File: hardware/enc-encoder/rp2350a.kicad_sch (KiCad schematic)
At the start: 31 parts, among them U1 RP2350A, U2 W25Q128JVS, Y1 ABM8-272-T3

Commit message: Needs checking and ERC fix
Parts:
- added TP1, TP2, TP3: SPARE_GPIO, TestPoint:TestPoint_Pad_1.0x1.0mm, symbol Connector:TestPoint
- renumbered C15 to C10, C12 to C11, C13 to C12, C14 to C13, C2 to C14, C1 to C15, C11 to C16, C9 to C17, C8 to C18, C21 to C20, C18 to C21, C20 to C22, C16 to C23, C17 to C24, C22 to C9, R13 to R12, R6 to R13, R12 to R14, R7 to R15, R15 to R16, R4 to R17, R5 to R18, R14 to R19, R3 to R20, U2 to U4, U1 to U5
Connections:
- net GPIO_0 is gone; now on net RP_I2C_SDA: R14.2
- net RP_HALL_DIR: now reaches U5.10 (GPIO7)
- net RP_ID_ADDR2: now reaches U5.12 (GPIO8)
- net RP_ID_ADDR1: now reaches U5.13 (GPIO9)
- net RP_ID_ADDR0: now reaches U5.14 (GPIO10)
- net at U5.15 (GPIO11): now also TP1.1
- net at U5.16 (GPIO12): now also TP2.1
- net at U5.17 (GPIO13): now also TP3.1
- net RP_I2C_SDA: now reaches U5.2 (GPIO0)
- net RP_I2C_SCL: now reaches U5.3 (GPIO1)
- net RP_RS485_RX: now reaches U5.4 (GPIO2)
- net RP_HALL_AOUT: now reaches U5.40 (GPIO26/ADC0)
- net RP_RS485_TX: now reaches U5.5 (GPIO3)
- net RP_RS485_DIR: now reaches U5.7 (GPIO4)
- net RP_STATUS_LED: now reaches U5.8 (GPIO5)
- net RP_HALL_PGO: now reaches U5.9 (GPIO6)
- no-connect marks 0 -> 15
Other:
- note added: "Flash mem"

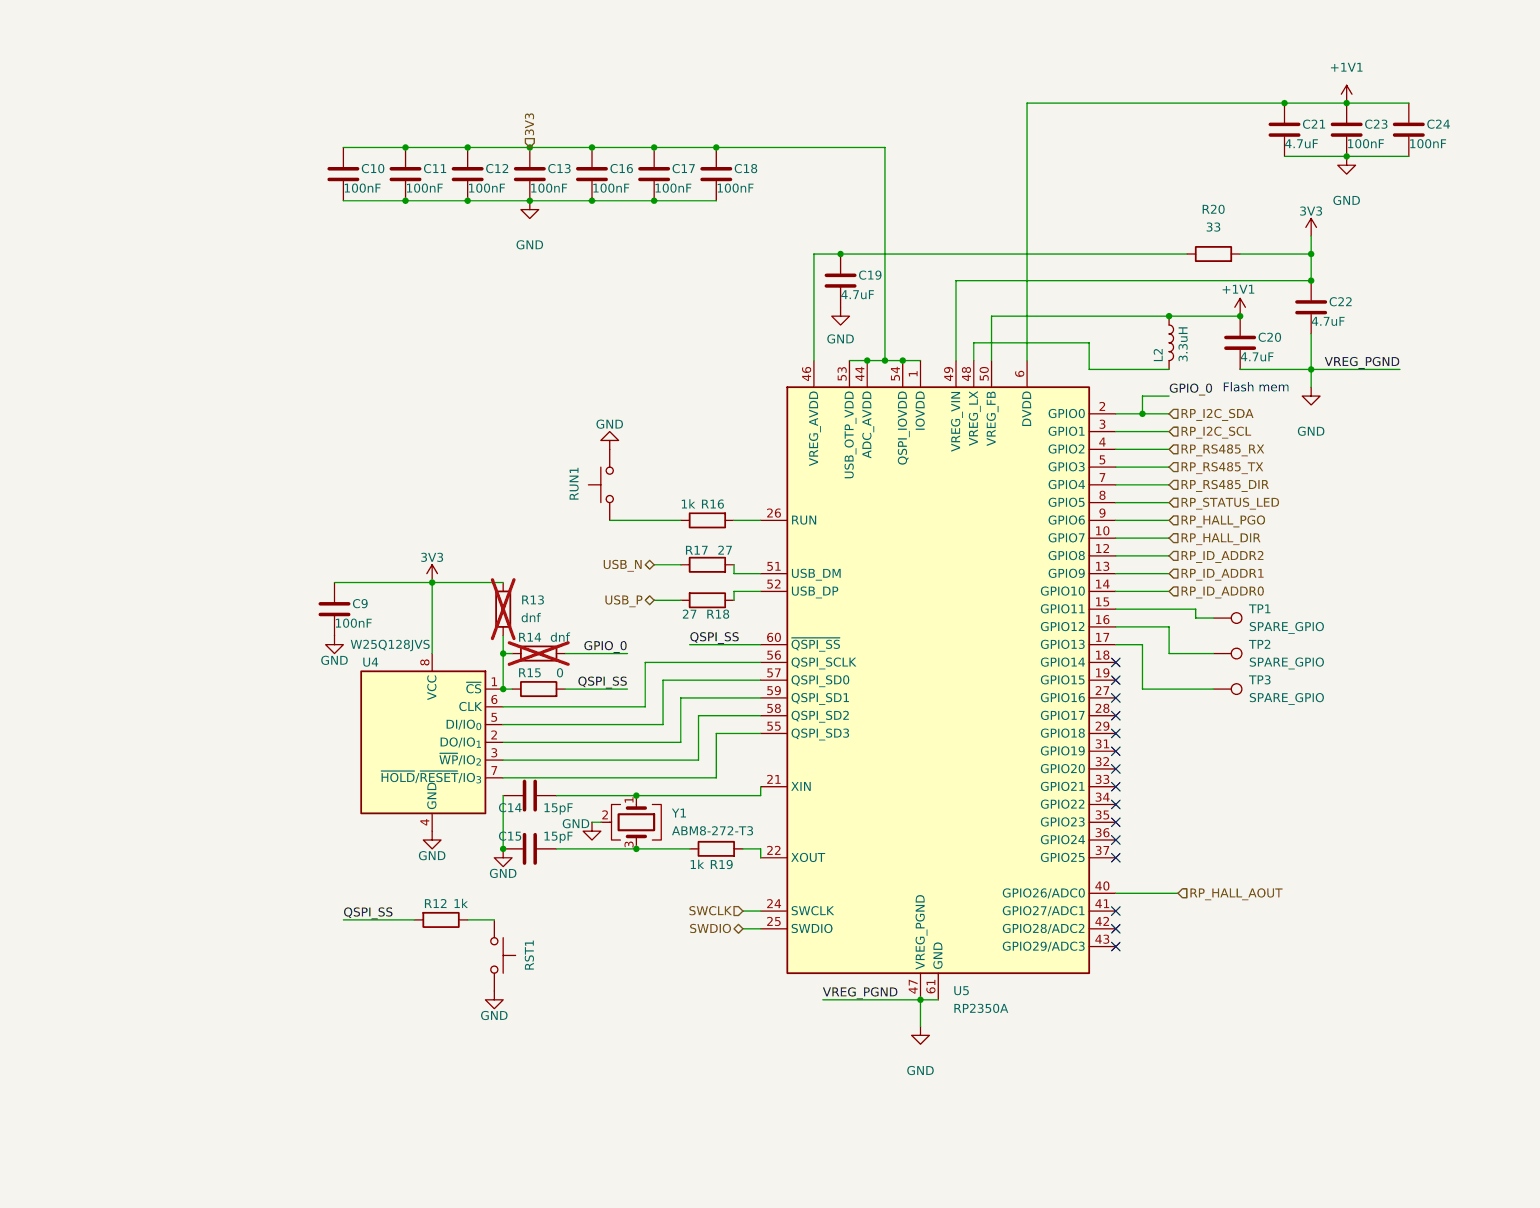
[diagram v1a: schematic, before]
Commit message: Feat: Fixed schematic errors, updated BOM
Fixed various schematic errors and missing footprints, models, symbols etc.
Also updated BOM to include active, available, appropriate components
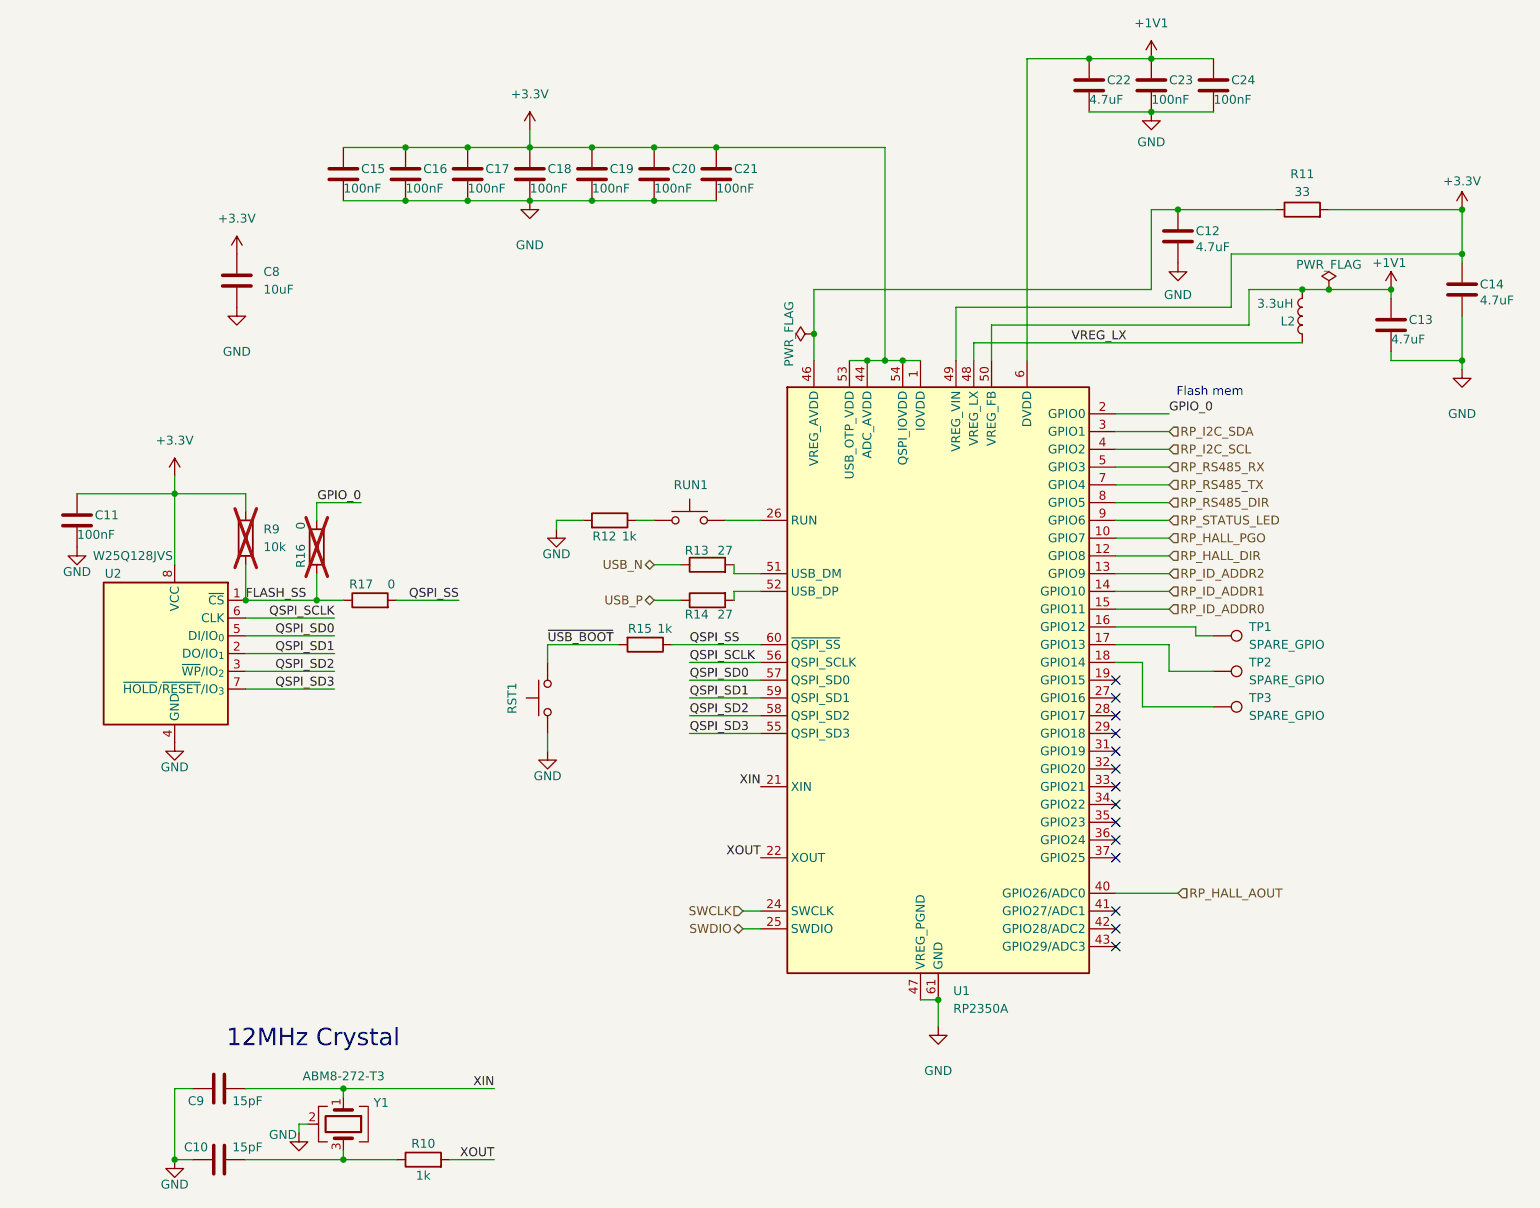
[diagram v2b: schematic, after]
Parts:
- removed C14, C15: 15pF, symbol Device:C
- removed R16, R19: 1k, symbol Device:R
- removed R18: 27, symbol Device:R
- removed U5: RP2350A, Package_DFN_QFN:QFN-60-1EP_7x7mm_P0.4mm_EP3.4x3.4mm, symbol MCU_RaspberryPi:RP2350A
- added C10, C9: 15pF, Capacitor_SMD:C_0402_1005Metric_Pad0.74x0.62mm_HandSolder, symbol Device:C
- added C8: 10uF, Capacitor_SMD:C_0805_2012Metric_Pad1.18x1.45mm_HandSolder, symbol Device:C
- added R10, R15: 1k, Resistor_SMD:R_0402_1005Metric_Pad0.72x0.64mm_HandSolder, symbol Device:R
- added R14: 27, Resistor_SMD:R_0402_1005Metric_Pad0.72x0.64mm_HandSolder, symbol Device:R
- added U1: RP2350A, Package_DFN_QFN:QFN-60-1EP_7x7mm_P0.4mm_EP3.4x3.4mm, symbol MCU_RaspberryPi:RP2350A
- C11: renamed from C9; footprint Capacitor_SMD:C_0603_1608Metric -> Capacitor_SMD:C_0402_1005Metric_Pad0.74x0.62mm_HandSolder; Supplier (none) -> DigiKey; Supplier Link (none) -> https://www.digikey.com.au/en/products/detail/murata-electr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; Supplier Part No (none) -> 490-10698-1-ND; distributors part number 1276-1012-2-ND -> (none); manufactuer part number CL10F104ZB8NNNC -> (none); manufacturer Samsung Electro-Mechanics -> (none)
- C12: renamed from C19; footprint Capacitor_SMD:C_0603_1608Metric -> Capacitor_SMD:C_0402_1005Metric_Pad0.74x0.62mm_HandSolder; Supplier (none) -> DigiKey; Supplier Link (none) -> https://www.digikey.com.au/en/products/detail/murata-electr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; Supplier Part No (none) -> 490-5915-1-ND
- C13: renamed from C20; footprint Capacitor_SMD:C_0603_1608Metric -> Capacitor_SMD:C_0402_1005Metric_Pad0.74x0.62mm_HandSolder; Supplier (none) -> DigiKey; Supplier Link (none) -> https://www.digikey.com.au/en/products/detail/murata-electr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; Supplier Part No (none) -> 490-5915-1-ND
- C14: renamed from C22; footprint Capacitor_SMD:C_0603_1608Metric -> Capacitor_SMD:C_0402_1005Metric_Pad0.74x0.62mm_HandSolder; Supplier (none) -> DigiKey; Supplier Link (none) -> https://www.digikey.com.au/en/products/detail/murata-electr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; Supplier Part No (none) -> 490-5915-1-ND
- C15: renamed from C10; footprint Capacitor_SMD:C_0603_1608Metric -> Capacitor_SMD:C_0402_1005Metric_Pad0.74x0.62mm_HandSolder; Supplier (none) -> DigiKey; Supplier Link (none) -> https://www.digikey.com.au/en/products/detail/murata-electr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; Supplier Part No (none) -> 490-10698-1-ND; distributors part number 1276-1012-2-ND -> (none); manufactuer part number CL10F104ZB8NNNC -> (none); manufacturer Samsung Electro-Mechanics -> (none)
- C16: renamed from C11; footprint Capacitor_SMD:C_0603_1608Metric -> Capacitor_SMD:C_0402_1005Metric_Pad0.74x0.62mm_HandSolder; Supplier (none) -> DigiKey; Supplier Link (none) -> https://www.digikey.com.au/en/products/detail/murata-electr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; Supplier Part No (none) -> 490-10698-1-ND; distributors part number 1276-1012-2-ND -> (none); manufactuer part number CL10F104ZB8NNNC -> (none); manufacturer Samsung Electro-Mechanics -> (none)
- C17: renamed from C12; footprint Capacitor_SMD:C_0603_1608Metric -> Capacitor_SMD:C_0402_1005Metric_Pad0.74x0.62mm_HandSolder; Supplier (none) -> DigiKey; Supplier Link (none) -> https://www.digikey.com.au/en/products/detail/murata-electr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; Supplier Part No (none) -> 490-10698-1-ND; distributors part number 1276-1012-2-ND -> (none); manufactuer part number CL10F104ZB8NNNC -> (none); manufacturer Samsung Electro-Mechanics -> (none)
- C18: renamed from C13; footprint Capacitor_SMD:C_0603_1608Metric -> Capacitor_SMD:C_0402_1005Metric_Pad0.74x0.62mm_HandSolder; Supplier (none) -> DigiKey; Supplier Link (none) -> https://www.digikey.com.au/en/products/detail/murata-electr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; Supplier Part No (none) -> 490-10698-1-ND; distributors part number 1276-1012-2-ND -> (none); manufactuer part number CL10F104ZB8NNNC -> (none); manufacturer Samsung Electro-Mechanics -> (none)
- C19: renamed from C16; footprint Capacitor_SMD:C_0603_1608Metric -> Capacitor_SMD:C_0402_1005Metric_Pad0.74x0.62mm_HandSolder; Supplier (none) -> DigiKey; Supplier Link (none) -> https://www.digikey.com.au/en/products/detail/murata-electr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; Supplier Part No (none) -> 490-10698-1-ND; distributors part number 1276-1012-2-ND -> (none); manufactuer part number CL10F104ZB8NNNC -> (none); manufacturer Samsung Electro-Mechanics -> (none)
- C20: renamed from C17; footprint Capacitor_SMD:C_0603_1608Metric -> Capacitor_SMD:C_0402_1005Metric_Pad0.74x0.62mm_HandSolder; Supplier (none) -> DigiKey; Supplier Link (none) -> https://www.digikey.com.au/en/products/detail/murata-electr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; Supplier Part No (none) -> 490-10698-1-ND; distributors part number 1276-1012-2-ND -> (none); manufactuer part number CL10F104ZB8NNNC -> (none); manufacturer Samsung Electro-Mechanics -> (none)
- C21: renamed from C18; footprint Capacitor_SMD:C_0603_1608Metric -> Capacitor_SMD:C_0402_1005Metric_Pad0.74x0.62mm_HandSolder; Supplier (none) -> DigiKey; Supplier Link (none) -> https://www.digikey.com.au/en/products/detail/murata-electr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; Supplier Part No (none) -> 490-10698-1-ND; distributors part number 1276-1012-2-ND -> (none); manufactuer part number CL10F104ZB8NNNC -> (none); manufacturer Samsung Electro-Mechanics -> (none)
- C22: renamed from C21; footprint Capacitor_SMD:C_0603_1608Metric -> Capacitor_SMD:C_0402_1005Metric_Pad0.74x0.62mm_HandSolder; Supplier (none) -> DigiKey; Supplier Link (none) -> https://www.digikey.com.au/en/products/detail/murata-electr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; Supplier Part No (none) -> 490-5915-1-ND
- C23, C24: footprint Capacitor_SMD:C_0603_1608Metric -> Capacitor_SMD:C_0402_1005Metric_Pad0.74x0.62mm_HandSolder; Supplier (none) -> DigiKey; Supplier Link (none) -> https://www.digikey.com.au/en/products/detail/murata-electr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; Supplier Part No (none) -> 490-10698-1-ND; distributors part number 1276-1012-2-ND -> (none); manufactuer part number CL10F104ZB8NNNC -> (none); manufacturer Samsung Electro-Mechanics -> (none)
- L2: Supplier (none) -> DigiKey; Supplier Link (none) -> https://www.digikey.com.au/en/products/detail/abracon-llc/A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; Supplier Part No (none) -> 535-AOTA-B201610S3R3-101-TCT-ND; distributors part number 535-AOTA-B201610S3R3-101-TTR-ND -> (none); manufactuer part number AOTA-B201610S3R3-101-T -> (none); manufacturer Abracon LLC -> (none)
- R11: renamed from R20; footprint (none) -> Resistor_SMD:R_0402_1005Metric_Pad0.72x0.64mm_HandSolder; Supplier (none) -> DigiKey; Supplier Link (none) -> https://www.digikey.com.au/en/products/detail/yageo/RC0402F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; Supplier Part No (none) -> 311-33.0LRCT-ND
- R12: footprint (none) -> Resistor_SMD:R_0402_1005Metric_Pad0.72x0.64mm_HandSolder; Supplier (none) -> DigiKey; Supplier Link (none) -> https://www.digikey.com.au/en/products/detail/yageo/RC0402F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; Supplier Part No (none) -> 311-1.00KLRCT-ND
- R13: renamed from R17; footprint (none) -> Resistor_SMD:R_0402_1005Metric_Pad0.72x0.64mm_HandSolder; Supplier (none) -> DigiKey; Supplier Link (none) -> https://www.digikey.com.au/en/products/detail/yageo/RC0402F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; Supplier Part No (none) -> YAG3086CT-ND
- R16: renamed from R14; value dnf -> 0; footprint (none) -> Resistor_SMD:R_0402_1005Metric_Pad0.72x0.64mm_HandSolder; Supplier (none) -> DigiKey; Supplier Part No (none) -> 311-0.0JRCT-ND
- R17: renamed from R15; footprint (none) -> Resistor_SMD:R_0402_1005Metric_Pad0.72x0.64mm_HandSolder; Supplier (none) -> DigiKey; Supplier Link (none) -> https://www.digikey.com.au/en/products/detail/yageo/RC0402J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; Supplier Part No (none) -> 311-0.0JRCT-ND
- R9: renamed from R13; value dnf -> 10k; footprint (none) -> Resistor_SMD:R_0402_1005Metric_Pad0.72x0.64mm_HandSolder; Supplier (none) -> DigiKey; Supplier Link (none) -> https://www.digikey.com.au/en/products/detail/yageo/RC0402F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; Supplier Part No (none) -> 311-10.0KLRCT-ND
- RST1, RUN1: Supplier (none) -> DigiKey; Supplier Link (none) -> https://www.digikey.com.au/en/products/detail/c-k/PTS636SKG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; Supplier Part No (none) -> CKN12324-1-ND; distributors part number CKN12324-2-ND -> (none); manufactuer part number GSPTS004302 -> (none); manufacturer C&K -> (none)
- TP1, TP2, TP3: now left out of the parts list
- U2: renamed from U4; Supplier (none) -> DigiKey; Supplier Link (none) -> https://www.digikey.com.au/en/products/detail/winbond-elect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; Supplier Part No (none) -> 256-W25Q128JVSIQTRCT-ND
- Y1: footprint (none) -> Crystal:Crystal_SMD_Abracon_ABM8G-4Pin_3.2x2.5mm; Supplier (none) -> DigiKey; Supplier Link (none) -> https://www.digikey.com.au/en/products/detail/abracon-llc/A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; Supplier Part No (none) -> 535-ABM8-272-T3CT-ND
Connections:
- net +1V1: now also L2.2, U1.23 (DVDD), U1.39 (DVDD), U1.50 (VREG_FB), U1.6 (DVDD); no longer L2.1
- net GND: now also R12.2, RST1.1, C10.1, C8.1, C9.1, U1.47 (VREG_PGND), U1.61 (GND); no longer RST1.2, RUN1.2
- net QSPI_SS: now also R15.1, U1.60 (~{QSPI_SS}); no longer R12.2
- net RP_HALL_AOUT: now also U1.40 (GPIO26/ADC0)
- net RP_HALL_DIR: now also U1.12 (GPIO8)
- net RP_HALL_PGO: now also U1.10 (GPIO7)
- net RP_I2C_SCL: now also U1.4 (GPIO2)
- net RP_I2C_SDA: now also U1.3 (GPIO1); no longer R16.2
- net RP_ID_ADDR0: now also U1.15 (GPIO11)
- net RP_ID_ADDR1: now also U1.14 (GPIO10)
- net RP_ID_ADDR2: now also U1.13 (GPIO9)
- net RP_RS485_DIR: now also U1.8 (GPIO5)
- net RP_RS485_RX: now also U1.5 (GPIO3)
- net RP_RS485_TX: now also U1.7 (GPIO4)
- net RP_STATUS_LED: now also U1.9 (GPIO6)
- net SWCLK: now also U1.24 (SWCLK)
- net SWDIO: now also U1.25 (SWDIO)
- net USB_P: now also R14.1
- net at R12.1: now also RUN1.1; no longer RST1.1
- net XIN: now reaches Y1.1
- net XIN: now also C9.2, U1.21 (XIN)
- net at Y1.3: now also C10.2, R10.1
- net at TP1.1: now also U1.16 (GPIO12)
- net at TP3.1: now also U1.18 (GPIO14)
- net at TP2.1: now also U1.17 (GPIO13)
- net FLASH_SS: now reaches R16.1, R17.1, R9.2, U2.1 (~{CS})
- net QSPI_SD1: now reaches U2.2 (DO/IO_{1})
- net QSPI_SD1: now also U1.59 (QSPI_SD1)
- net QSPI_SD2: now reaches U2.3 (~{WP}/IO_{2})
- net QSPI_SD2: now also U1.58 (QSPI_SD2)
- net QSPI_SD0: now reaches U2.5 (DI/IO_{0})
- net QSPI_SD0: now also U1.57 (QSPI_SD0)
- net QSPI_SCLK: now reaches U2.6 (CLK)
- net QSPI_SCLK: now also U1.56 (QSPI_SCLK)
- net QSPI_SD3: now reaches U2.7 (~{HOLD}/~{RESET}/IO_{3})
- net QSPI_SD3: now also U1.55 (QSPI_SD3)
- net at C12.1, R11.1: now also U1.46 (VREG_AVDD)
- net at R13.2: now also U1.51 (USB_DM)
- net 3V3 renamed +3.3V
- net +3.3V: now also C8.2, U1.1 (IOVDD), U1.11 (IOVDD), U1.20 (IOVDD), U1.30 (IOVDD), U1.38 (IOVDD), U1.44 (ADC_AVDD), U1.45 (IOVDD), U1.49 (VREG_VIN), U1.53 (USB_OTP_VDD), U1.54 (QSPI_IOVDD)
- new net: RUN1.2, U1.26 (RUN)
- new net: R14.2, U1.52 (USB_DP)
- new net GPIO_0: R16.2, U1.2 (GPIO0)
- new net VREG_LX: L2.1, U1.48 (VREG_LX)
- new net XOUT: R10.2, U1.22 (XOUT)
- new net ~{USB_BOOT}: R15.2, RST1.2
- no-connect marks 15 -> 14
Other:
- note added: "12MHz Crystal"
- moved on the sheet: C11, C12, C13, C14, C22, C23, C24, L2, R11, R16, R17, R9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

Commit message: Feat: Updated sheet names and titles
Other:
- title: (none) -> RP2350A Microprocessor
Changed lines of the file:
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@@
 	(generator_version "10.0")
 	(paper "A4")
+	(title_block
+		(title "RP2350A Microprocessor")
+		(date "2026-08-15")
+		(rev "V1R1")
+	)
 	(text "Flash mem"
 		(exclude_from_sim no)

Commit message: Feat: Encoder PCB microcontroller layout
Finished microcontroller layout requirements. Additionally fixed schematic BOM and other footprints.
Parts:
- C12, C13, C14: footprint Capacitor_SMD:C_0402_1005Metric_Pad0.74x0.62mm_HandSolder -> SMD:C_0402_1005Metric_small
- L2: footprint Inductor_SMD:L_0805_2012Metric_Pad1.05x1.20mm_HandSolder -> SMD:L_Abracon_AOTA-B201610S3R3-101-T
- R11: footprint Resistor_SMD:R_0402_1005Metric_Pad0.72x0.64mm_HandSolder -> SMD:R_0402_1005Metric_small
- U1: footprint Package_DFN_QFN:QFN-60-1EP_7x7mm_P0.4mm_EP3.4x3.4mm -> SMD:RP2350A-QFN-60-1EP_7x7mm_P0.4mm_EP3.4x3.4mm
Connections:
- net +1V1: now also L2.1; no longer L2.2
- net RP_HALL_DIR: no longer U1.12 (GPIO8)
- net RP_RS485_DIR: no longer U1.8 (GPIO5)
- net RP_RS485_RX: no longer U1.5 (GPIO3)
- net RP_RS485_TX: no longer U1.7 (GPIO4)
- net VREG_LX: now also L2.2; no longer L2.1
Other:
- moved on the sheet: L2

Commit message: Feat: Encoder PCB Power layout and routing
Added 3.3V voltage regulator traces and routing to the board
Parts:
- renumbered RST1 to RST, RUN1 to RUN
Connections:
- net RP_HALL_DIR: now also U1.12 (GPIO8)
- net RP_HALL_PGO: now also U1.5 (GPIO3); no longer U1.10 (GPIO7)
- net RP_I2C_SCL: now also U1.3 (GPIO1); no longer U1.4 (GPIO2)
- net RP_I2C_SDA: now also U1.4 (GPIO2); no longer U1.3 (GPIO1)
- net RP_RS485_DIR: now also U1.10 (GPIO7)
- net RP_RS485_RX: now also U1.8 (GPIO5)
- net RP_RS485_TX: now also U1.9 (GPIO6)
- net RP_STATUS_LED: now also U1.7 (GPIO4); no longer U1.9 (GPIO6)
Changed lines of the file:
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@@
 		)
 	)
-	(hierarchical_label "RP_HALL_DIR"
-		(shape input)
-		(at 176.53 78.74 0)
-		(effects
-			(font
-				(size 1.27 1.27)
-			)
-			(justify left)
-		)
-	)
-	(hierarchical_label "RP_I2C_SCL"
+	(hierarchical_label "RP_HALL_PGO"
 		(shape input)
-		(at 172.72 76.2 0)
+		(at 172.72 78.74 0)
 		(effects
 			(font
@@
 		)
 	)
-	(hierarchical_label "RP_ID_ADDR2"
-		(shape input)
-		(at 172.72 93.98 0)
-		(effects
-			(font
-				(size 1.27 1.27)
-			)
-			(justify left)
-		)
-	)
 	(hierarchical_label "USB_N"
 		(shape bidirectional)
@@
 		)
 	)
-	(hierarchical_label "RP_HALL_AOUT"
+	(hierarchical_label "RP_STATUS_LED"
 		(shape input)
-		(at 173.99 139.7 0)
+		(at 172.72 81.28 0)
 		(effects
 			(font
@@
 		)
 	)
-	(hierarchical_label "RP_STATUS_LED"
+	(hierarchical_label "RP_HALL_DIR"
 		(shape input)
-		(at 172.72 86.36 0)
+		(at 172.72 91.44 0)
 		(effects
 			(font
@@
 		)
 	)
-	(hierarchical_label "RP_I2C_SDA"
+	(hierarchical_label "RP_HALL_AOUT"
+		(shape input)
+		(at 173.99 139.7 0)
+		(effects
+			(font
+				(size 1.27 1.27)
+			)
+			(justify left)
+		)
+	)
+	(hierarchical_label "RP_I2C_SCL"
 		(shape input)
 		(at 172.72 73.66 0)
@@
 		)
 	)
-	(hierarchical_label "RP_HALL_PGO"
+	(hierarchical_label "RP_I2C_SDA"
 		(shape input)
-		(at 172.72 88.9 0)
+		(at 172.72 76.2 0)
 		(effects
 			(font
@@
 		)
 	)
-	(hierarchical_label "RP_ID_ADDR0"
+	(hierarchical_label "RP_ID_ADDR2"
 		(shape input)
-		(at 172.72 99.06 0)
+		(at 172.72 93.98 0)
 		(effects
 			(font
@@
 	(hierarchical_label "RP_RS485_TX"
 		(shape input)
-		(at 190.5 91.44 0)
+		(at 172.72 86.36 0)
+		(effects
+			(font
+				(size 1.27 1.27)
+			)
+			(justify left)
+		)
+	)
+	(hierarchical_label "RP_ID_ADDR0"
+		(shape input)
+		(at 172.72 99.06 0)
 		(effects
 			(font
@@
 	(hierarchical_label "RP_RS485_DIR"
 		(shape input)
-		(at 190.5 93.98 0)
+		(at 172.72 88.9 0)
 		(effects
 			(font
@@
 	(hierarchical_label "RP_RS485_RX"
 		(shape input)
-		(at 190.5 88.9 0)
+		(at 172.72 83.82 0)
 		(effects
 			(font
@@
 		(in_pos_files yes)
 		(dnp no)
-		(property "Reference" "RST1"
+		(property "Reference" "RST"
 			(at 79.502 114.046 0)
 			(show_name no)
@@
 			(project "enc-encoder"
 				(path "/830e855f-c01b-4865-ac3f-fca5cbe32ffd/772c9f81-7e5d-44a6-ac7a-4279420baea9"
-					(reference "RST1")
+					(reference "RST")
 					(unit 1)
 				)
@@
 		(in_pos_files yes)
 		(dnp no)
-		(property "Reference" "RUN1"
+		(property "Reference" "RUN"
 			(at 101.854 82.042 0)
 			(show_name no)
@@
 			(project "enc-encoder"
 				(path "/830e855f-c01b-4865-ac3f-fca5cbe32ffd/772c9f81-7e5d-44a6-ac7a-4279420baea9"
-					(reference "RUN1")
+					(reference "RUN")
 					(unit 1)
 				)

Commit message: Feat: Finished Encoder PCB Routing
Finished PCB routing for the EnC magnetic encoder. Some minor improvements and fabrication markings still needed
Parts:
- TP1, TP2, TP3: footprint TestPoint:TestPoint_Pad_1.0x1.0mm -> TestPoint:TestPoint_Pad_D1.0mm
- renumbered RST to RST1, RUN to RUN1
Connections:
- net RP_RS485_DIR: now also U1.9 (GPIO6); no longer U1.10 (GPIO7)
- net RP_RS485_TX: now also U1.10 (GPIO7); no longer U1.9 (GPIO6)
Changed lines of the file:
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@@
 		)
 	)
-	(hierarchical_label "RP_ID_ADDR1"
+	(hierarchical_label "RP_RS485_TX"
 		(shape input)
-		(at 172.72 96.52 0)
+		(at 172.72 88.9 0)
 		(effects
 			(font
@@
 		)
 	)
-	(hierarchical_label "RP_ID_ADDR2"
+	(hierarchical_label "RP_ID_ADDR1"
 		(shape input)
-		(at 172.72 93.98 0)
+		(at 172.72 96.52 0)
 		(effects
 			(font
@@
 		)
 	)
-	(hierarchical_label "RP_RS485_TX"
+	(hierarchical_label "RP_ID_ADDR2"
 		(shape input)
-		(at 172.72 86.36 0)
+		(at 172.72 93.98 0)
 		(effects
 			(font
@@
 	(hierarchical_label "RP_RS485_DIR"
 		(shape input)
-		(at 172.72 88.9 0)
+		(at 172.72 86.36 0)
 		(effects
 			(font
@@
 			)
 		)
-		(property "Footprint" "TestPoint:TestPoint_Pad_1.0x1.0mm"
+		(property "Footprint" "TestPoint:TestPoint_Pad_D1.0mm"
 			(at 179.07 107.95 0)
 			(hide yes)
@@
 			)
 		)
-		(property "Footprint" "TestPoint:TestPoint_Pad_1.0x1.0mm"
+		(property "Footprint" "TestPoint:TestPoint_Pad_D1.0mm"
 			(at 179.07 118.11 0)
 			(hide yes)
@@
 			)
 		)
-		(property "Footprint" "TestPoint:TestPoint_Pad_1.0x1.0mm"
+		(property "Footprint" "TestPoint:TestPoint_Pad_D1.0mm"
 			(at 179.07 113.03 0)
 			(hide yes)
@@
 		(in_pos_files yes)
 		(dnp no)
-		(property "Reference" "RST"
+		(property "Reference" "RST1"
 			(at 79.502 114.046 0)
 			(show_name no)
@@
 			(project "enc-encoder"
 				(path "/830e855f-c01b-4865-ac3f-fca5cbe32ffd/772c9f81-7e5d-44a6-ac7a-4279420baea9"
-					(reference "RST")
+					(reference "RST1")
 					(unit 1)
 				)
@@
 		(in_pos_files yes)
 		(dnp no)
-		(property "Reference" "RUN"
+		(property "Reference" "RUN1"
 			(at 101.854 82.042 0)
 			(show_name no)
@@
 			(project "enc-encoder"
 				(path "/830e855f-c01b-4865-ac3f-fca5cbe32ffd/772c9f81-7e5d-44a6-ac7a-4279420baea9"
-					(reference "RUN")
+					(reference "RUN1")
 					(unit 1)
 				)

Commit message: Feat: Flipped encoder to backside of PCB
Flipped AS5600 magnetic sensor to backside of board. This allows proper magnet distancing (0.5-3mm) while maintaining component clearances. Cost difference is neglible.
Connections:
- net RP_HALL_PGO: now also U1.3 (GPIO1); no longer U1.5 (GPIO3)
- net RP_I2C_SCL: now also U1.5 (GPIO3); no longer U1.3 (GPIO1)
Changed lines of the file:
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@@
 		)
 	)
-	(hierarchical_label "RP_HALL_PGO"
+	(hierarchical_label "RP_I2C_SCL"
 		(shape input)
 		(at 172.72 78.74 0)
@@
 		)
 	)
-	(hierarchical_label "RP_I2C_SCL"
+	(hierarchical_label "RP_HALL_PGO"
 		(shape input)
 		(at 172.72 73.66 0)
